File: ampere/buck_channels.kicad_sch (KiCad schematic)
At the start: 123 parts, among them J2 Channel 1, J3 Channel 2, J4 Channel 3, U10 TPS55289, U12 INA238, U13 INA238, U14 INA238, U6 TPS55289, U8 TPS55289

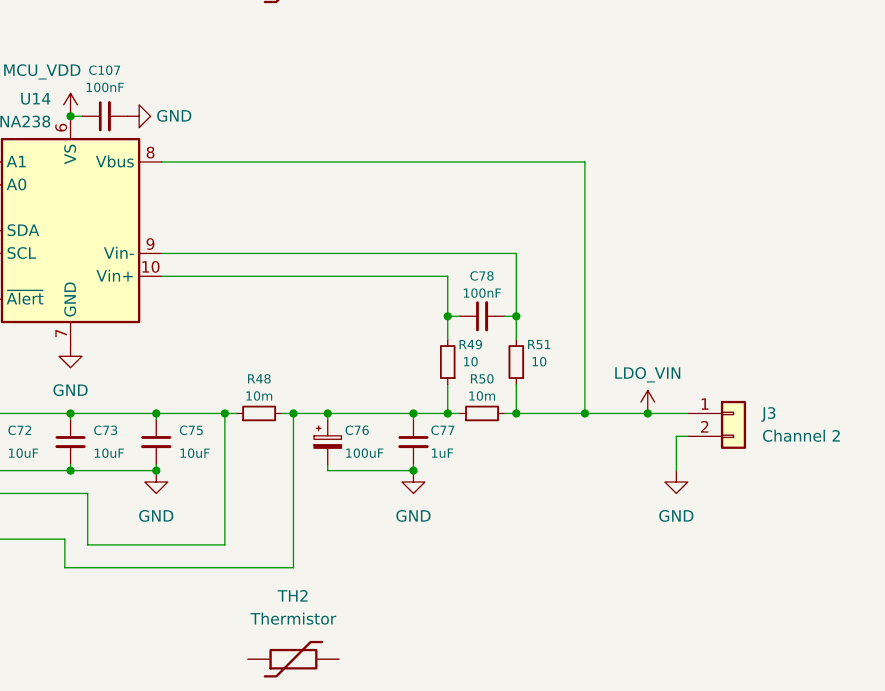
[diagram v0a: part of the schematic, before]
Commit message: LM74502 implementation v1
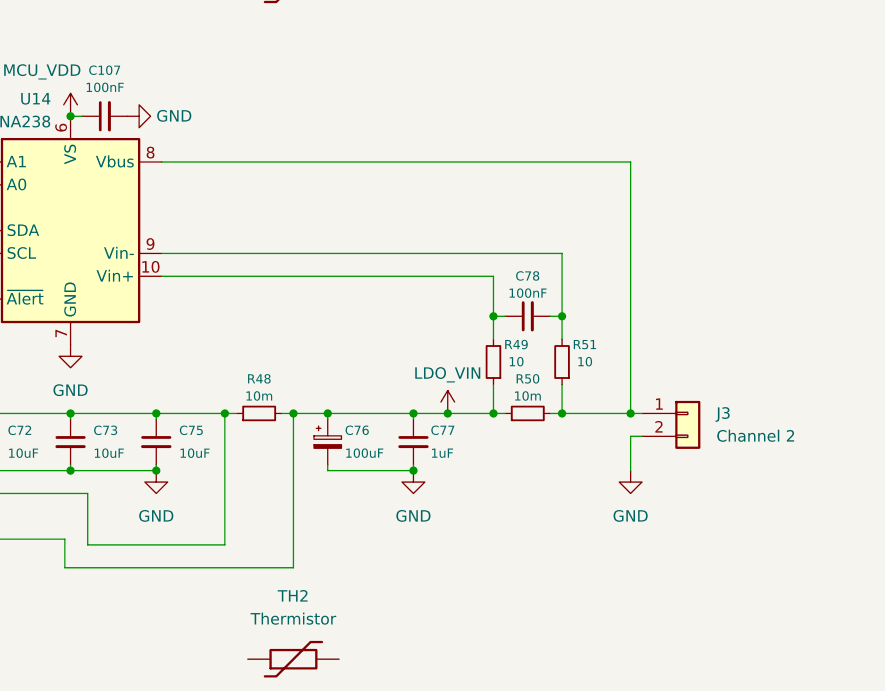
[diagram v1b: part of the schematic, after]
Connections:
- net LDO_VIN: now also C76.1, C77.1, R47.2, R48.2, R49.1, R50.1; no longer J3.1 (Pin_1), R50.2, R51.1, U14.8 (Vbus)
- new net: J3.1 (Pin_1), R50.2, R51.1, U14.8 (Vbus)
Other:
- moved on the sheet: C78, J3, R49, R50, R51

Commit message: connect i2c up
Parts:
- removed J2: Channel 1, Connector:Banana_Jack_2Pin, symbol Connector_Generic:Conn_01x02
- removed J3: Channel 2, Connector:Banana_Jack_2Pin, symbol Connector_Generic:Conn_01x02
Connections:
- net MODE is gone; now on net GND: U10.2 (MODE), U6.2 (MODE), U8.2 (MODE)
- net GND: now also U13.1 (A1), U13.2 (A0), U14.1 (A1), U14.2 (A0)
- net VIN: no longer C41.1, C42.1, C43.1, C44.1, C45.1, C50.1, C55.1, C56.1, C57.1, C58.1, C61.1, C63.1, U6.7 (VIN), U8.7 (VIN)
- new net PPHV: C41.1, C42.1, C43.1, C44.1, C45.1, C50.1, C55.1, C56.1, C57.1, C58.1, C61.1, C63.1, U6.7 (VIN), U8.7 (VIN)
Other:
- note added: "0x40"
- note added: "0x75"

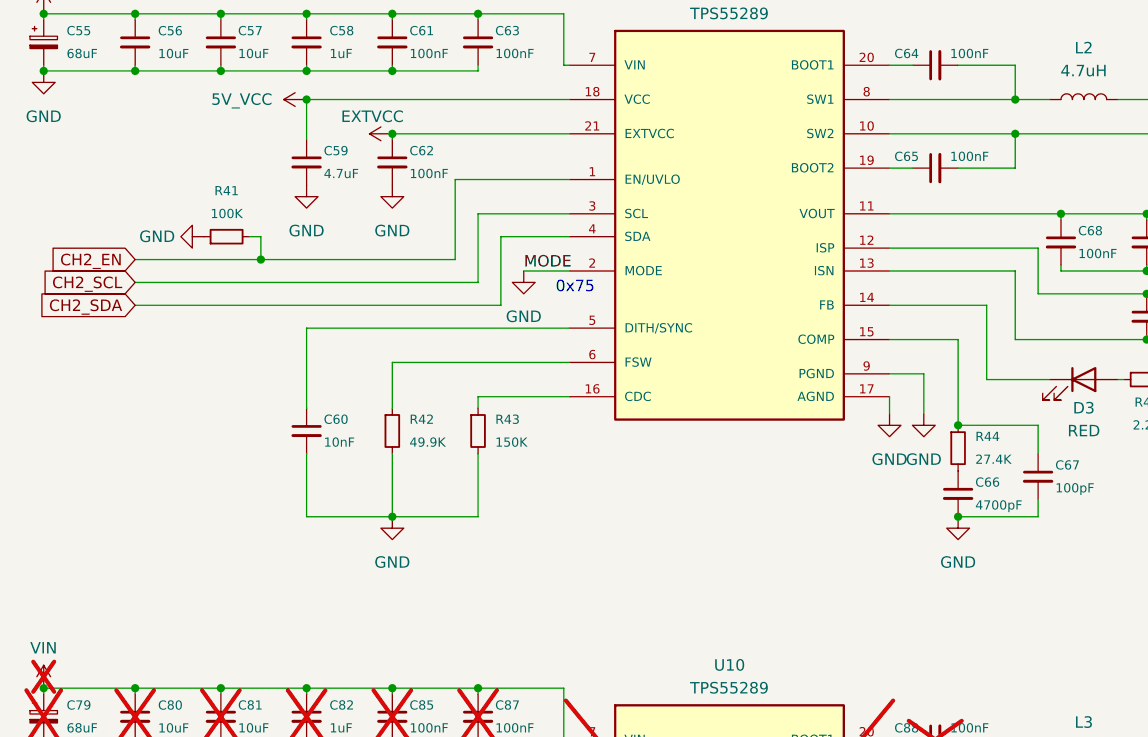
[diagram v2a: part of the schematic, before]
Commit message: begin implementing AGND retrofit
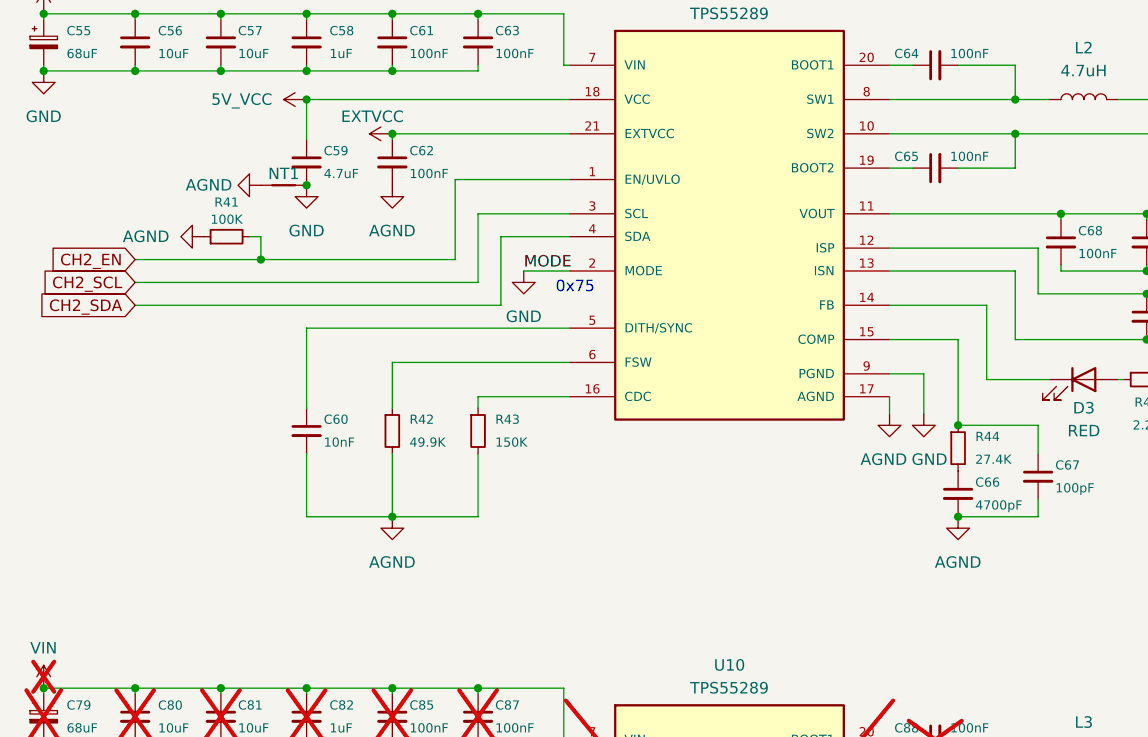
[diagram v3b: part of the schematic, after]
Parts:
- added NT1: NetTie_2, NetTie:NetTie-2_SMD_Pad0.5mm, symbol Device:NetTie_2
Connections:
- net GND: now also NT1.2; no longer C60.2, C62.2, C66.2, C67.2, R41.1, R42.2, R43.2, U8.17 (AGND)
- new net AGND: C60.2, C62.2, C66.2, C67.2, NT1.1, R41.1, R42.2, R43.2, U8.17 (AGND)

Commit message: first production run generation, edit vias
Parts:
- added NT2: NetTie_2, NetTie:NetTie-2_SMD_Pad0.5mm, symbol Device:NetTie_2
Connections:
- net AGND: now also C40.2, C47.2, C48.2, C49.2, R33.2, R34.2, R37.1, U6.17 (AGND), NT2.1
- net GND: now also NT2.2; no longer C40.2, C47.2, C48.2, C49.2, R33.2, R34.2, R37.1, U6.17 (AGND)
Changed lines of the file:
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@@
 	(title_block
 		(title "Buck-Boost Regulator Channels")
+		(rev "B")
 		(comment 1 "Brian Guan")
 		(comment 2 "INA238")
@@
 	)
 	(junction
+		(at 129.54 69.215)
+		(diameter 0)
+		(color 0 0 0 0)
+	)
+	(junction
 		(at 232.41 153.67)
 		(diameter 0)
@@
 		(in_pos_files yes)
 		(dnp no)
-		(fields_autoplaced yes)
 		(property "Reference" "R37"
-			(at 120.65 69.85 90)
+			(at 120.65 71.12 90)
 			(show_name no)
 			(do_not_autoplace no)
@@
 		)
 		(property "Value" "100K"
-			(at 120.65 72.39 90)
+			(at 120.65 73.025 90)
 			(show_name no)
 			(do_not_autoplace no)
@@
 	)
 	(symbol
+		(lib_id "power:GND")
+		(at 124.46 69.215 270)
+		(unit 1)
+		(body_style 1)
+		(exclude_from_sim no)
+		(in_bom yes)
+		(on_board yes)
+		(in_pos_files yes)
+		(dnp no)
+		(fields_autoplaced yes)
+		(property "Reference" "#PWR0195"
+			(at 118.11 69.215 0)
+			(hide yes)
+			(show_name no)
+			(do_not_autoplace no)
+			(effects
+				(font
+					(size 1.27 1.27)
+				)
+			)
+		)
+		(property "Value" "AGND"
+			(at 121.285 69.2149 90)
+			(show_name no)
+			(do_not_autoplace no)
+			(effects
+				(font
+					(size 1.27 1.27)
+				)
+				(justify right)
+			)
+		)
+		(property "Footprint" ""
+			(at 124.46 69.215 0)
+			(hide yes)
+			(show_name no)
+			(do_not_autoplace no)
+			(effects
+				(font
+					(size 1.27 1.27)
+				)
+			)
+		)
+		(property "Datasheet" ""
+			(at 124.46 69.215 0)
+			(hide yes)
+			(show_name no)
+			(do_not_autoplace no)
+			(effects
+				(font
+					(size 1.27 1.27)
+				)
+			)
+		)
+		(property "Description" "Power symbol creates a global label with name \"GND\" , ground"
+			(at 124.46 69.215 0)
+			(hide yes)
+			(show_name no)
+			(do_not_autoplace no)
+			(effects
+				(font
+					(size 1.27 1.27)
+				)
+			)
+		)
+		(pin "1"
+		)
+		(instances
+			(project "ampere"
+				(path "/329c36c3-da44-49fd-8f70-d92646be88d6"
+					(reference "#PWR0195")
+					(unit 1)
+				)
+			)
+		)
+	)
+	(symbol
 		(lib_id "power:VCC")
 		(at 139.065 138.43 90)
@@
 			)
 		)
-		(property "Value" "GND"
+		(property "Value" "AGND"
 			(at 201.93 111.125 0)
 			(show_name no)
@@
 	)
 	(symbol
+		(lib_id "Device:NetTie_2")
+		(at 127 69.215 0)
+		(unit 1)
+		(body_style 1)
+		(exclude_from_sim no)
+		(in_bom no)
+		(on_board yes)
+		(in_pos_files yes)
+		(dnp no)
+		(property "Reference" "NT2"
+			(at 126.365 67.945 0)
+			(show_name no)
+			(do_not_autoplace no)
+			(effects
+				(font
+					(size 1.27 1.27)
+				)
+			)
+		)
+		(property "Value" "NetTie_2"
+			(at 127 67.31 0)
+			(hide yes)
+			(show_name no)
+			(do_not_autoplace no)
+			(effects
+				(font
+					(size 1.27 1.27)
+				)
+			)
+		)
+		(property "Footprint" "NetTie:NetTie-2_SMD_Pad0.5mm"
+			(at 127 69.215 0)
+			(hide yes)
+			(show_name no)
+			(do_not_autoplace no)
+			(effects
+				(font
+					(size 1.27 1.27)
+				)
+			)
+		)
+		(property "Datasheet" ""
+			(at 127 69.215 0)
+			(hide yes)
+			(show_name no)
+			(do_not_autoplace no)
+			(effects
+				(font
+					(size 1.27 1.27)
+				)
+			)
+		)
+		(property "Description" "Net tie, 2 pins"
+			(at 127 69.215 0)
+			(hide yes)
+			(show_name no)
+			(do_not_autoplace no)
+			(effects
+				(font
+					(size 1.27 1.27)
+				)
+			)
+		)
+		(pin "2"
+		)
+		(pin "1"
+		)
+		(instances
+			(project "ampere"
+				(path "/329c36c3-da44-49fd-8f70-d92646be88d6"
+					(reference "NT2")
+					(unit 1)
+				)
+			)
+		)
+	)
+	(symbol
 		(lib_id "Device:Thermistor")
 		(at 276.225 174.625 90)
@@
 			)
 		)
-		(property "Value" "GND"
+		(property "Value" "AGND"
 			(at 139.065 111.125 0)
 			(show_name no)
@@
 			)
 		)
-		(property "Value" "GND"
+		(property "Value" "AGND"
 			(at 114.935 74.9299 90)
 			(show_name no)
@@
 		(in_pos_files yes)
 		(dnp no)
-		(fields_autoplaced yes)
 		(property "Reference" "#PWR070"
 			(at 198.12 100.965 0)
@@
 		)
 		(property "Value" "GND"
-			(at 198.12 99.695 0)
+			(at 198.755 99.695 0)
 			(show_name no)
 			(do_not_autoplace no)
@@
 			)
 		)
-		(property "Value" "GND"
+		(property "Value" "AGND"
 			(at 139.065 74.295 0)
 			(show_name no)
@@
 		(in_pos_files yes)
 		(dnp no)
-		(fields_autoplaced yes)
 		(property "Reference" "#PWR069"
 			(at 194.31 100.965 0)
@@
 			)
 		)
-		(property "Value" "GND"
-			(at 194.31 99.695 0)
+		(property "Value" "AGND"
+			(at 193.675 99.695 0)
 			(show_name no)
 			(do_not_autoplace no)
@@
 		(dnp no)
 		(property "Reference" "NT1"
-			(at 127 142.875 0)
+			(at 126.365 142.875 0)
 			(show_name no)
 			(do_not_autoplace no)

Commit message: mark moisture detection as DNP, fix enable pulldowns
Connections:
- net EXTVCC is gone; now on net 5V_VCC: C40.1, C62.1, C86.1, U10.21 (EXTVCC), U6.21 (EXTVCC), U8.21 (EXTVCC)
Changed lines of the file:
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@@
 	)
 	(junction
+		(at 139.065 59.69)
+		(diameter 0)
+		(color 0 0 0 0)
+	)
+	(junction
 		(at 280.035 72.39)
 		(diameter 0)
@@
 	)
 	(junction
+		(at 139.065 134.62)
+		(diameter 0)
+		(color 0 0 0 0)
+	)
+	(junction
 		(at 129.54 200.025)
 		(diameter 0)
@@
 	(wire
 		(pts
+			(xy 139.065 134.62) (xy 129.54 134.62)
+		)
+		(stroke
+			(width 0)
+			(type default)
+		)
+	)
+	(wire
+		(pts
 			(xy 139.065 213.36) (xy 139.065 213.995)
 		)
@@
 	(wire
 		(pts
+			(xy 139.065 59.69) (xy 139.065 63.5)
+		)
+		(stroke
+			(width 0)
+			(type default)
+		)
+	)
+	(wire
+		(pts
 			(xy 158.75 205.74) (xy 158.115 205.74)
 		)
@@
 	(wire
 		(pts
-			(xy 158.75 134.62) (xy 129.54 134.62)
+			(xy 158.75 134.62) (xy 139.065 134.62)
 		)
 		(stroke
@@
 	(wire
 		(pts
-			(xy 158.75 59.69) (xy 129.54 59.69)
+			(xy 158.75 59.69) (xy 139.065 59.69)
 		)
 		(stroke
@@
 	(wire
 		(pts
+			(xy 139.065 59.69) (xy 129.54 59.69)
+		)
+		(stroke
+			(width 0)
+			(type default)
+		)
+	)
+	(wire
+		(pts
 			(xy 129.54 106.045) (xy 139.065 106.045)
 		)
@@
 	(wire
 		(pts
+			(xy 139.065 134.62) (xy 139.065 138.43)
+		)
+		(stroke
+			(width 0)
+			(type default)
+		)
+	)
+	(wire
+		(pts
 			(xy 201.93 130.81) (xy 208.28 130.81)
 		)
@@
 		)
 		(property "Value" "EXTVCC"
-			(at 140.335 136.525 90)
+			(at 149.86 136.525 90)
 			(show_name no)
 			(do_not_autoplace no)
@@
 		)
 		(property "Value" "EXTVCC"
-			(at 140.335 61.595 90)
+			(at 147.955 61.595 90)
 			(show_name no)
 			(do_not_autoplace no)
